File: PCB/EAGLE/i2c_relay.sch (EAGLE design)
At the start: 60 parts, among them IC1 PCF8575TS_1,118, K1 G3MB-202PL-DC5, K2 G3MB-202PL-DC5, K3 G3MB-202PL-DC5, K4 G3MB-202PL-DC5, K5 G3MB-202PL-DC5, K6 G3MB-202PL-DC5, K7 G3MB-202PL-DC5, K8 G3MB-202PL-DC5, Q1 MMST2222A-7-F, Q2 MMST2222A-7-F, Q3 MMST2222A-7-F, Q4 MMST2222A-7-F, Q5 MMST2222A-7-F, Q6 MMST2222A-7-F, Q7 MMST2222A-7-F, Q8 MMST2222A-7-F

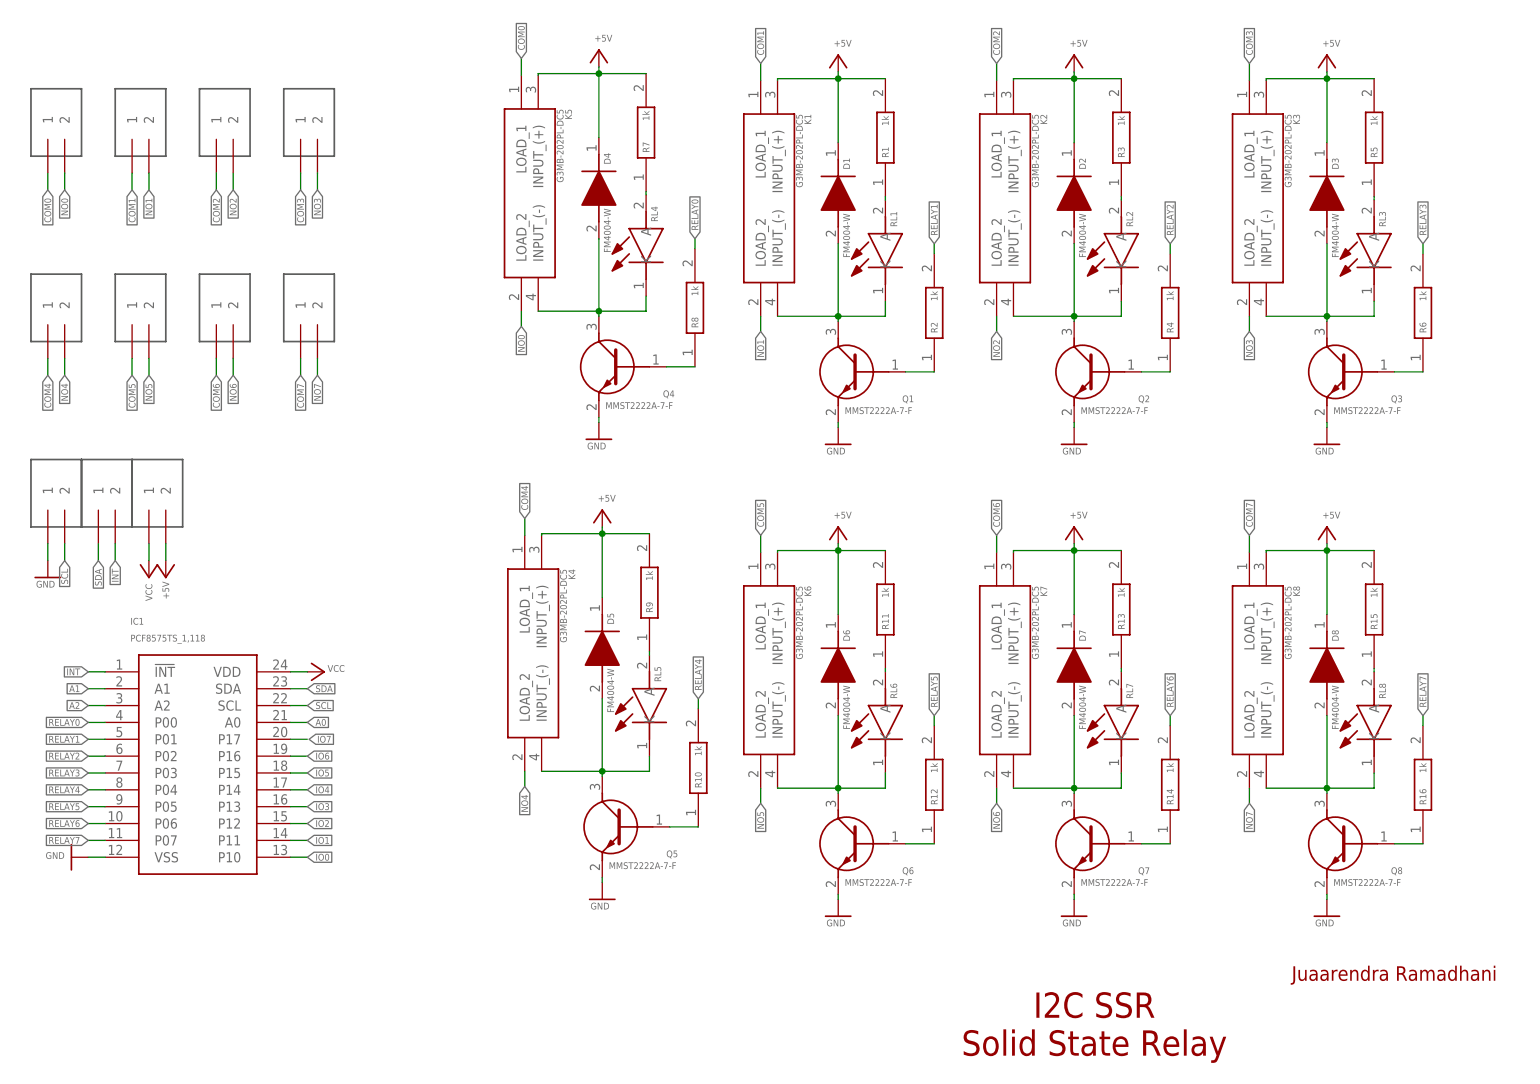
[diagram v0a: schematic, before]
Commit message: FEAT: add 3d and push to FUSION360
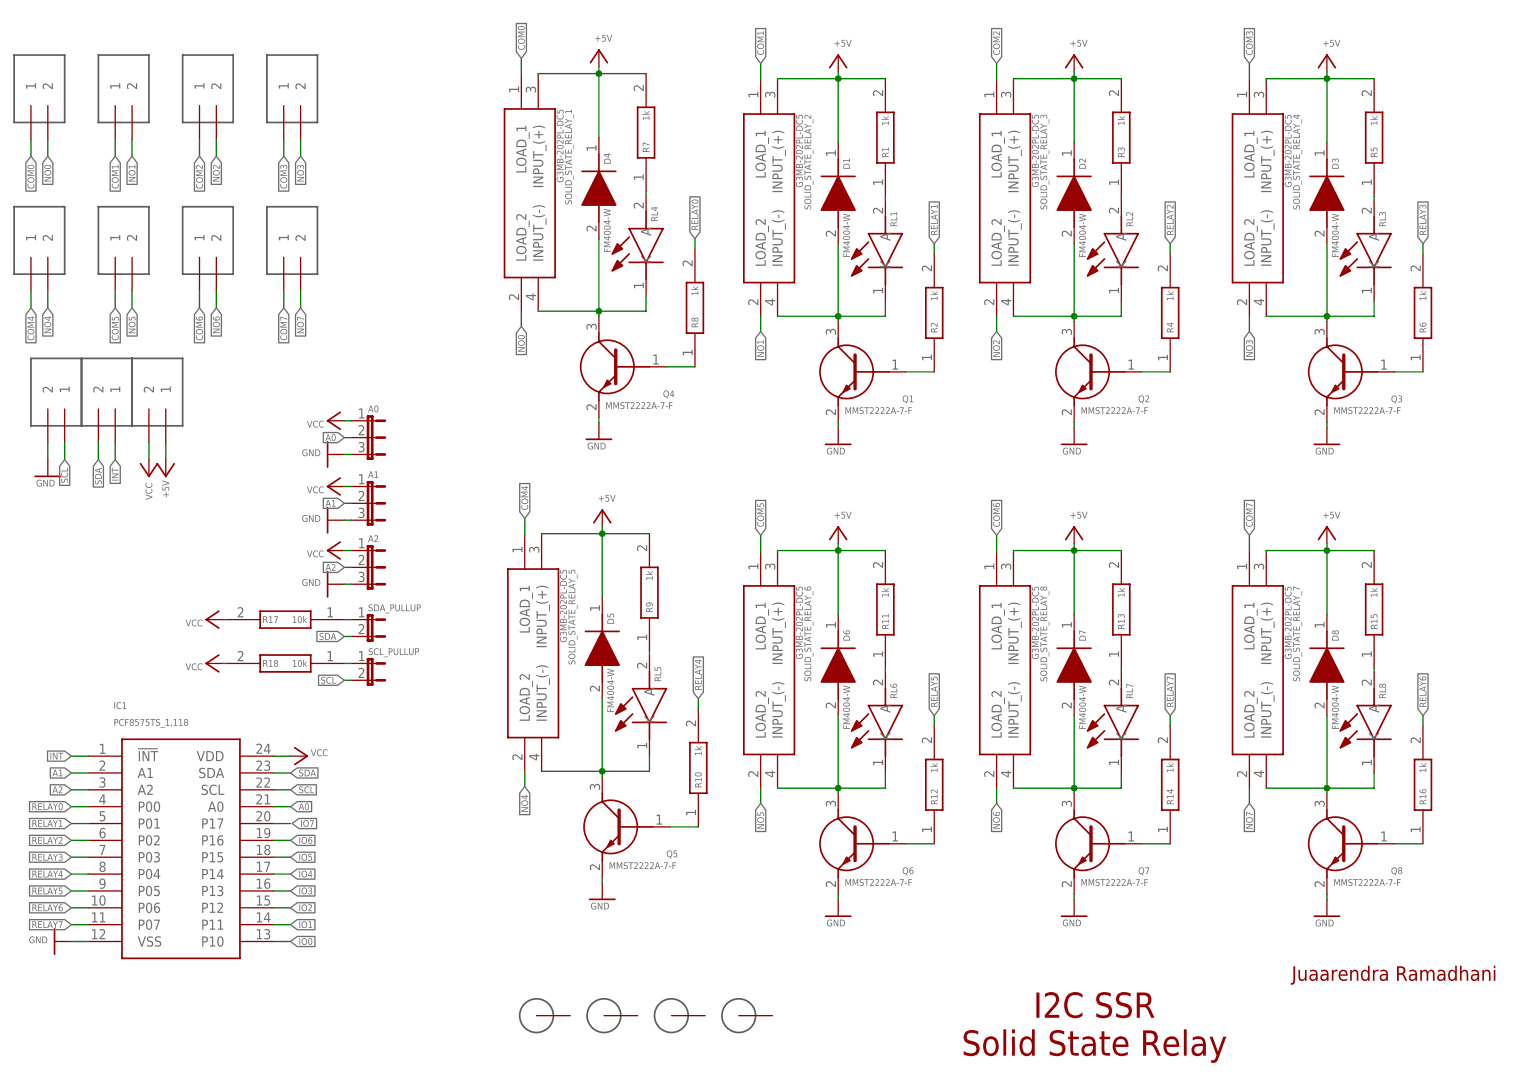
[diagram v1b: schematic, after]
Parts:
- added A0, A1, A2: (no value), jumper:JP2E
- added H1, H2, H3, H4: 3MM_HOLE, 3mm_special_hole:3MM_HOLE
- added R17, R18: 10k, AccesControlNFC:ESR03EZPJ103
- added SCL_PULLUP, SDA_PULLUP: (no value), jumper:JP1E
- renumbered K1 to SOLID_STATE_RELAY_2, K2 to SOLID_STATE_RELAY_3, K3 to SOLID_STATE_RELAY_4, K4 to SOLID_STATE_RELAY_5, K5 to SOLID_STATE_RELAY_1, K6 to SOLID_STATE_RELAY_6, K7 to SOLID_STATE_RELAY_8, K8 to SOLID_STATE_RELAY_7
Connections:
- new net N$25: R17.1, SDA_PULLUP.1
- new net N$27: R18.1, SCL_PULLUP.1
- net +5V: now also U$11.1; no longer U$11.2
- net A0: now also A0.2
- net A1: now also A1.2
- net A2: now also A2.2
- net GND: now also A0.3, A1.3, A2.3, U$9.2; no longer U$9.1
- net INT: now also U$10.1; no longer U$10.2
- net RELAY6: now also R16.2; no longer R14.2
- net RELAY7: now also R14.2; no longer R16.2
- net SCL: now also SCL_PULLUP.2, U$9.1; no longer U$9.2
- net SDA: now also SDA_PULLUP.2, U$10.2; no longer U$10.1
- net VCC: now also A0.1, A1.1, A2.1, R17.2, R18.2, U$11.2; no longer U$11.1
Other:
- moved on the sheet: IC1
